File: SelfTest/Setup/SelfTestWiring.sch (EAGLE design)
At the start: 5 parts

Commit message: Hardware: ^7 testing
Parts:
- added D4: YE, D-LED:LED5MM
- D2: value RD -> YE
- R1: value 47 -> 50
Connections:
- net RD renamed OG
- removed net 12V_SLA: BM3.BAT
- removed net 21V@150MA: BM3.PV
- removed net BK: BM3.16MA@0, BM3.DIO3, BM3.DIO4, D1.A
- removed net N$2: BM3.0V, R1.1
- removed net N$5: BM3.20MA@2, BM3.DIO12, BM3.DIO13, D2.A
- removed net YE: BM3.20MA@0, BM3.ADC0, D2.K, D3.K, R1.2
- new net 12V8@200MA: BM3.PWR
- new net BL: BM3.17MA@0, BM3.DIO4, D1.A
- new net BN: BM3.20MA@2, BM3.DIO10, BM3.DIO3, D4.A
- new net N$1: BM3.0V@3, R1.2
- new net VT: BM3.20MA@1, BM3.ADC0, D2.K, D3.K, D4.K, R1.1
- new net WH: BM3.20MA@3, BM3.DIO12, BM3.DIO13, D2.A
- net GN: now also BM3.20MA@0; no longer BM3.20MA@1, BM3.DIO10
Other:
- moved on the sheet: D2, D3, R1

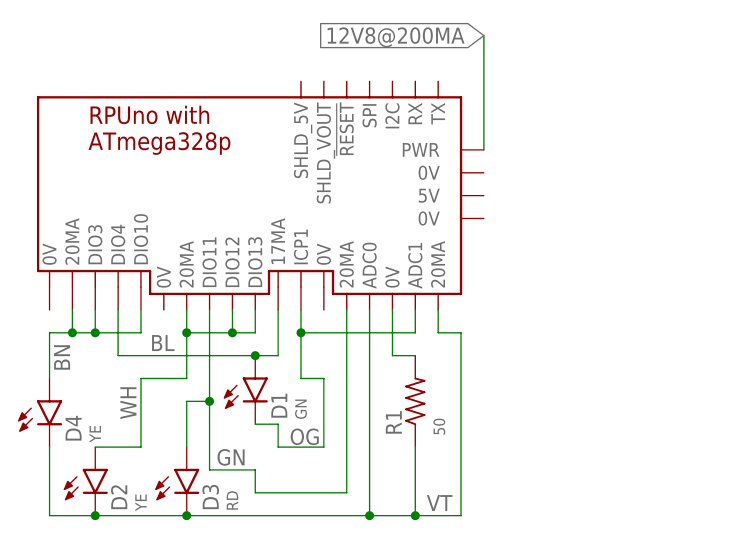
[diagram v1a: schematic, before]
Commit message: SelfTest: update for ^9
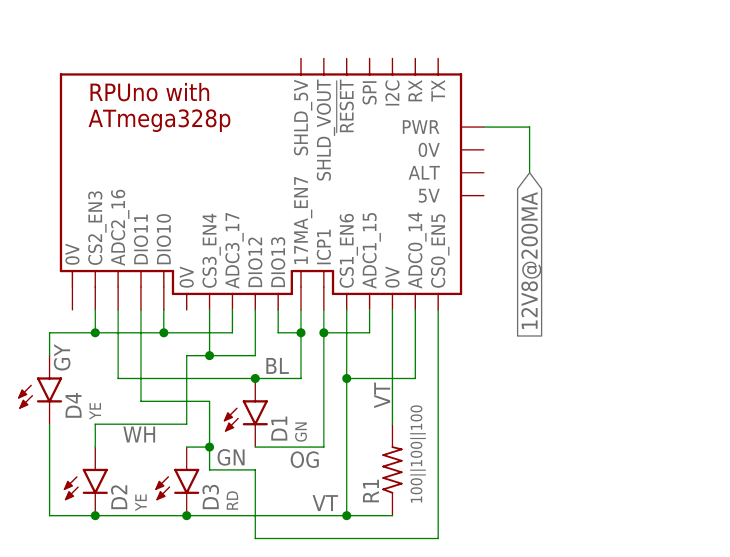
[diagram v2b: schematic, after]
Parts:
- R1: value 50 -> 100||100||100
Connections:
- removed net BN: BM3.20MA@2, BM3.DIO10, BM3.DIO3, D4.A
- new net GY: BM3.ADC3_17, BM3.CS2_EN3, BM3.DIO10, D4.A
- net BL: now also BM3.17MA_EN7, BM3.ADC2_16, BM3.DIO13; no longer BM3.17MA@0, BM3.DIO4
- net GN: now also BM3.CS0_EN5; no longer BM3.20MA@0
- net OG: now also BM3.ADC1_15; no longer BM3.ADC1
- net VT: now also BM3.ADC0_14, BM3.CS1_EN6; no longer BM3.20MA@1, BM3.ADC0
- net WH: now also BM3.CS3_EN4; no longer BM3.20MA@3, BM3.DIO13
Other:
- moved on the sheet: D1, D4, R1
